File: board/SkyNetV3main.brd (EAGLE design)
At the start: 160 x 100 mm, 61 parts, among them IC1 HC_05, IC2 RF4463PRO, IC3 LPC1768, IC4 BCX17, IC5 TPS63001, IC6 MCP73871-2CCI/ML, Q1 32.768KHz, Q2 12MHz, Q3 IRLM6402, Q4 BSS138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

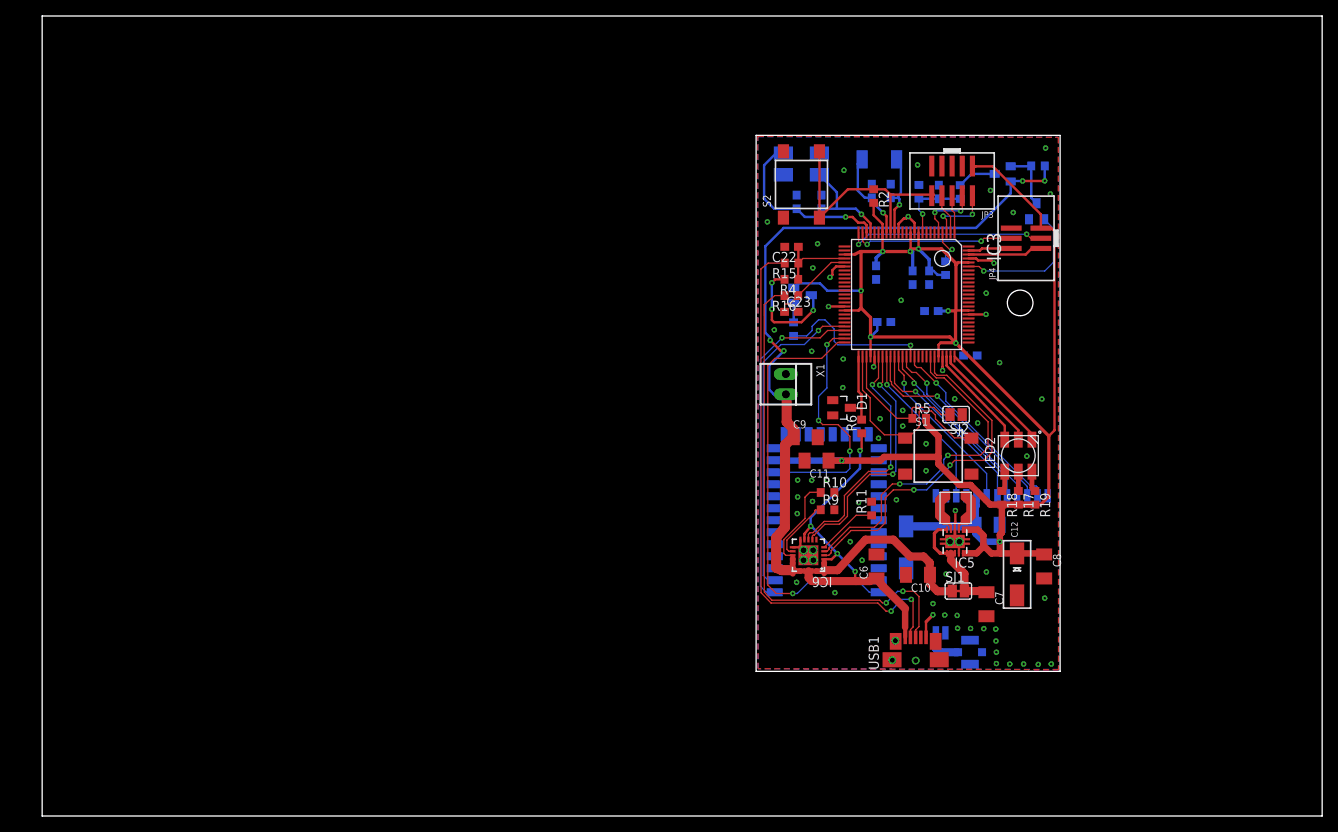
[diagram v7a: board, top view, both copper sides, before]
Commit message: corrected USB connector in layout+schematics
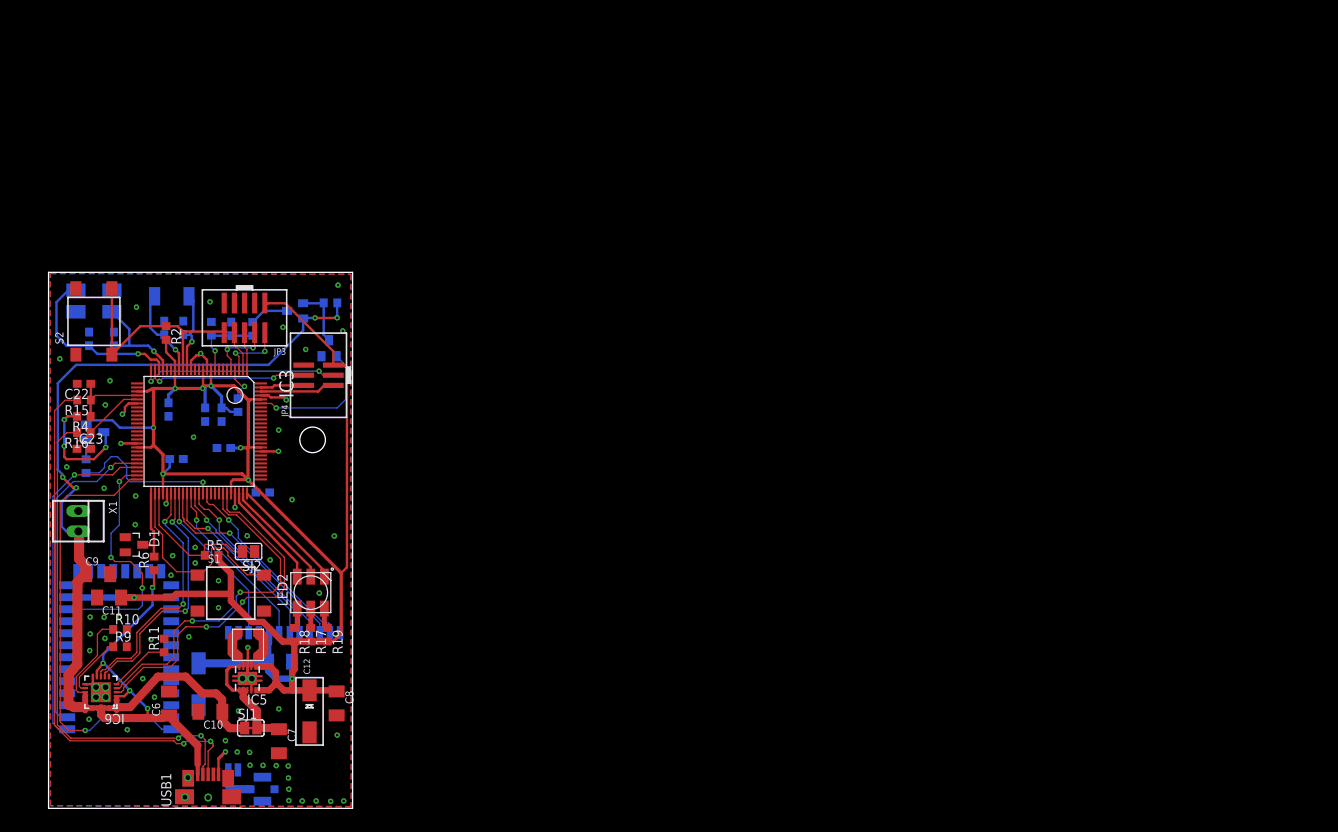
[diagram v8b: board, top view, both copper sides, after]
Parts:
- moved C1 90.1 mm to (29.7, 19.3)
- moved C10 90.1 mm to (21.0, 13.0)
- moved C11 90.1 mm to (8.36, 27.3)
- moved C12 90.1 mm to (33.4, 13.1)
- moved C13 90.1 mm to (19.6, 16.5)
- moved C16 90.1 mm to (22.7, 46.0)
- moved C17 90.1 mm to (16.8, 44.6)
- moved C21 90.1 mm to (15.8, 50.8)
- moved C22 90.1 mm to (5.23, 54.0)
- moved C23 90.1 mm to (5.21, 45.9)
- moved C6 90.1 mm to (15.8, 14.1)
- moved C7 90.1 mm to (29.6, 9.35)
- moved C8 90.1 mm to (36.8, 14.1)
- moved IC1 90.1 mm to (9.48, 14.7)
- moved IC3 90.1 mm to (19.6, 48.1)
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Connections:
- removed net USB-D+_IN: R15.2, USB1.2
- removed net USB-D-_IN: R16.2, USB1.3
- new net N$2: R16.2, USB1.2
- new net N$3: R15.2, USB1.3
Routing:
- net USB-D+_IN: track 69.1 -> 0.00 mm, vias 2 -> 0
- net N$3: track 0.00 -> 67.8 mm, vias 0 -> 2
- net USB-D-_IN: track 65.0 -> 0.00 mm, vias 2 -> 0
- net N$2: track 0.00 -> 62.2 mm, vias 0 -> 2
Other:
- board size 160 x 100 mm -> 38 x 67 mm
- board text removed: "14650"
- board text removed: "2x 18650"
